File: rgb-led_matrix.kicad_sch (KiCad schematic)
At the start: 0 parts

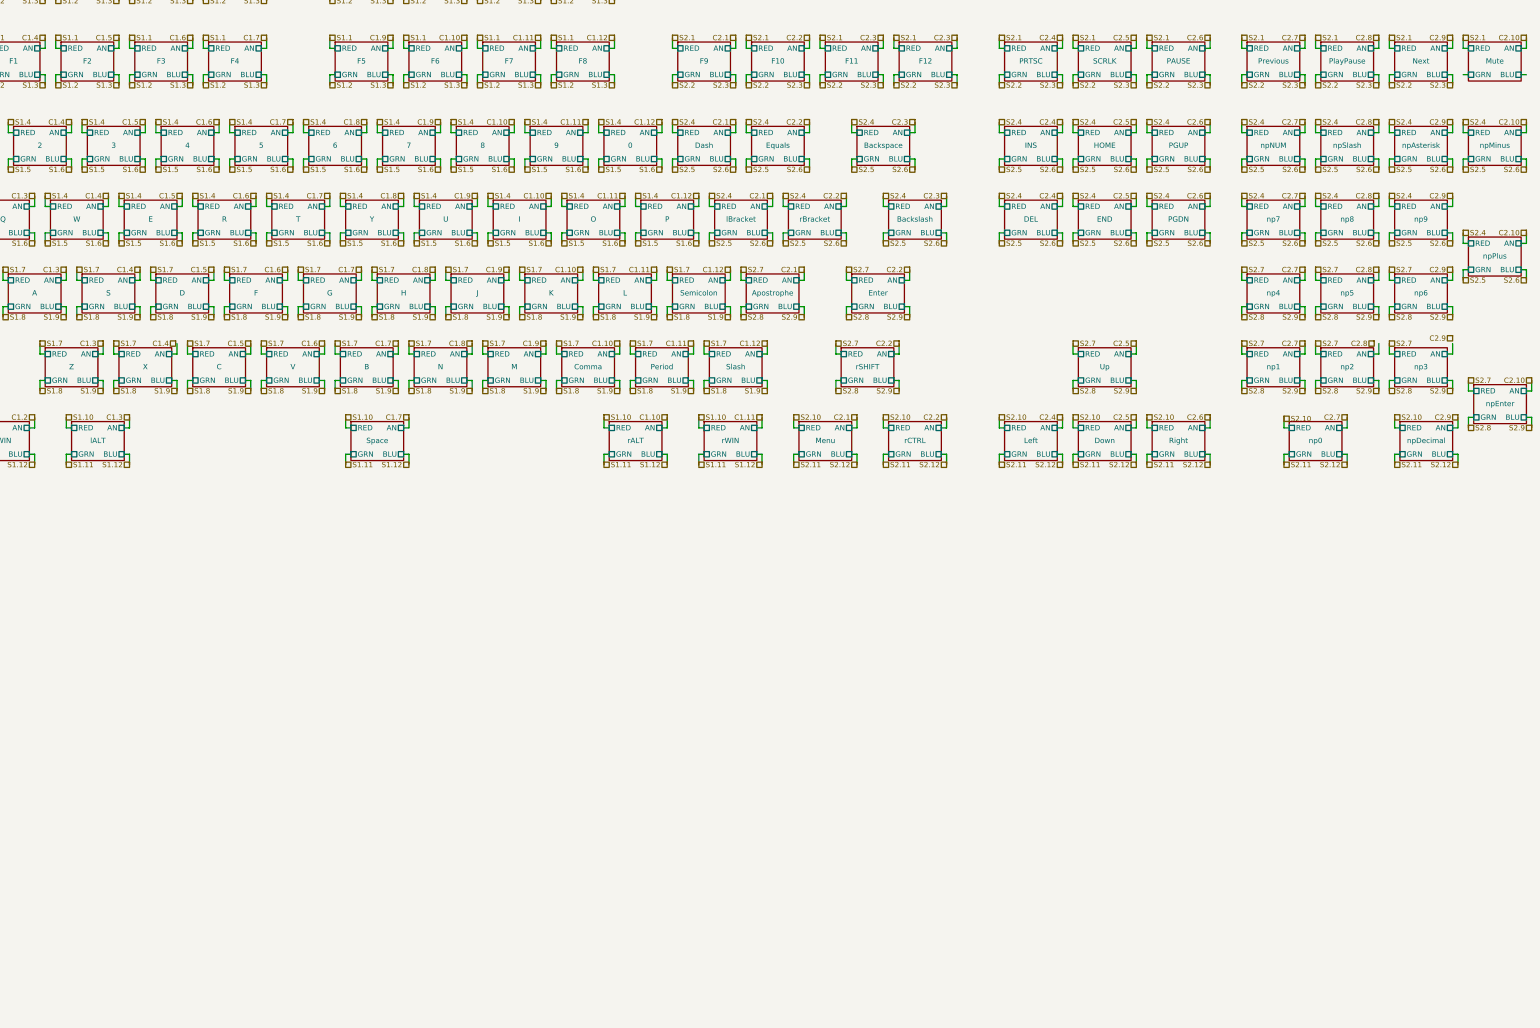
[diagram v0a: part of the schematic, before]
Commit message: Minor pcb layout changes. Add matrix led drivers
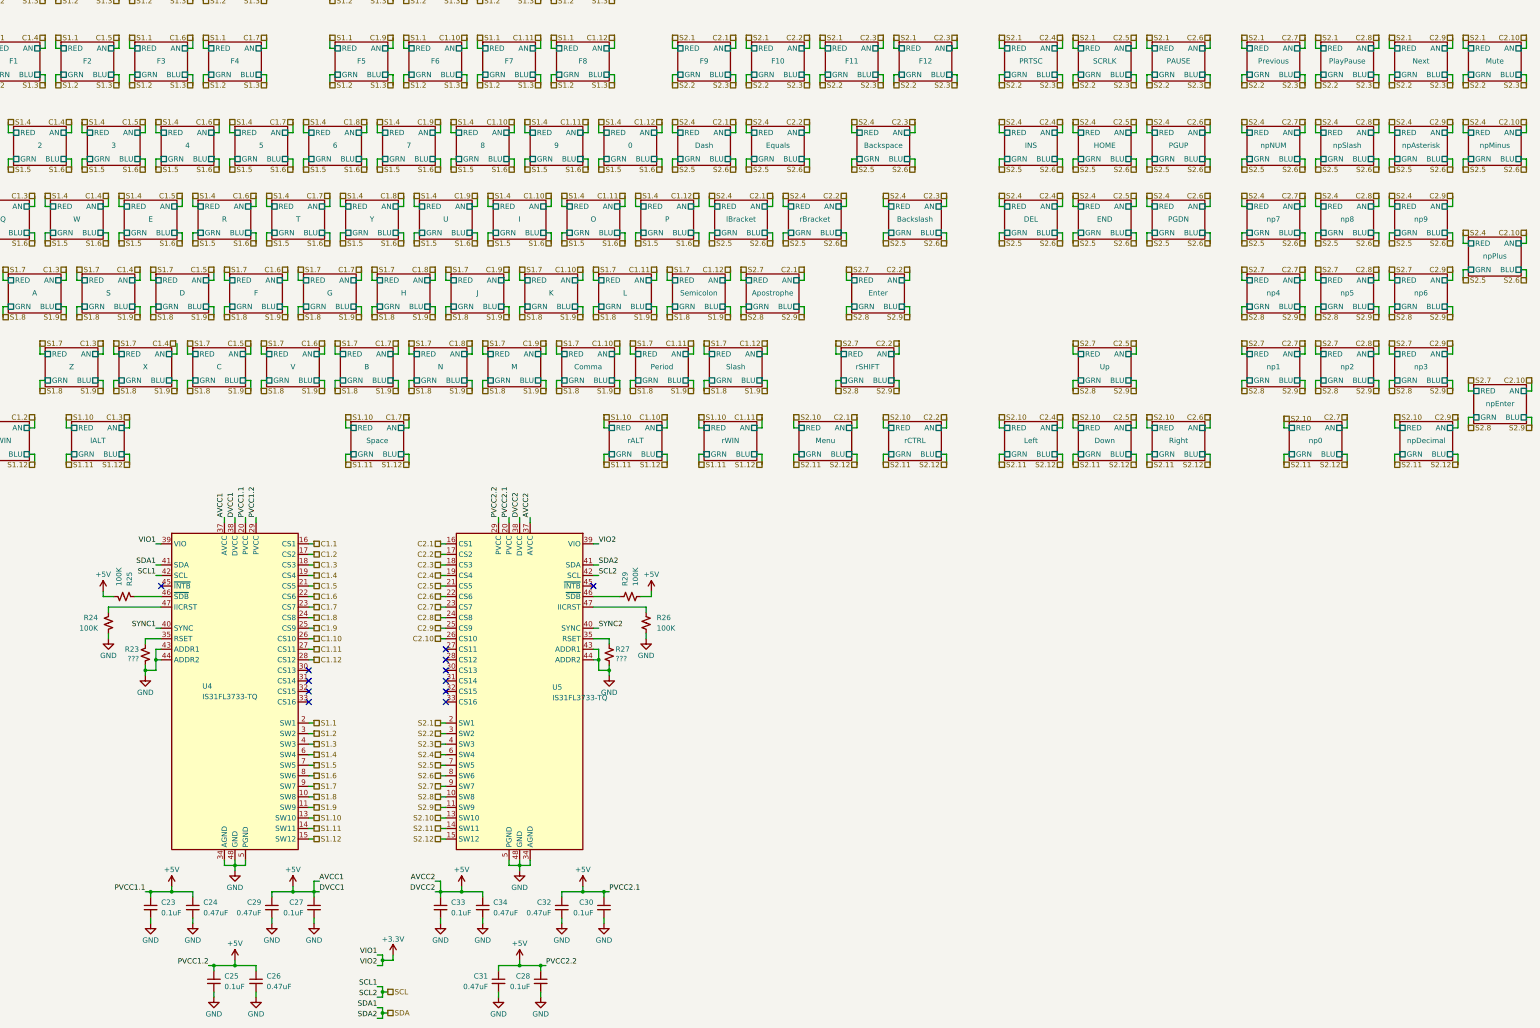
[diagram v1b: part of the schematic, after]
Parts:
- added C23, C25, C27, C28, C30, C33: 0.1uF, symbol Device:C_Small
- added C24, C26, C29, C31, C32, C34: 0.47uF, symbol Device:C_Small
- added R23, R27: ???, symbol Device:R_Small_US
- added R24, R25, R26, R29: 100K, symbol Device:R_Small_US
- added U4, U5: IS31FL3733-TQ, Package_QFP:TQFP-48-1EP_7x7mm_P0.5mm_EP5x5mm, symbol Driver_LED:IS31FL3733-TQ
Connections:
- net C1.1: now also U4.16 (CS1)
- net C1.10: now also U4.26 (CS10)
- net C1.11: now also U4.27 (CS11)
- net C1.12: now also U4.28 (CS12)
- net C1.2: now also U4.17 (CS2)
- net C1.3: now also U4.18 (CS3)
- net C1.4: now also U4.19 (CS4)
- net C1.5: now also U4.21 (CS5)
- net C1.6: now also U4.22 (CS6)
- net C1.7: now also U4.23 (CS7)
- net C1.8: now also U4.24 (CS8)
- net C1.9: now also U4.25 (CS9)
- net C2.1: now also U5.16 (CS1)
- net C2.10: now also U5.26 (CS10)
- net C2.2: now also U5.17 (CS2)
- net C2.3: now also U5.18 (CS3)
- net C2.4: now also U5.19 (CS4)
- net C2.5: now also U5.21 (CS5)
- net C2.6: now also U5.22 (CS6)
- net C2.7: now also U5.23 (CS7)
- net C2.8: now also U5.24 (CS8)
- net C2.9: now also U5.25 (CS9)
- net S1.1: now also U4.2 (SW1)
- net S1.10: now also U4.13 (SW10)
- net S1.11: now also U4.14 (SW11)
- net S1.12: now also U4.15 (SW12)
- net S1.2: now also U4.3 (SW2)
- net S1.3: now also U4.4 (SW3)
- net S1.4: now also U4.6 (SW4)
- net S1.5: now also U4.7 (SW5)
- net S1.6: now also U4.8 (SW6)
- net S1.7: now also U4.9 (SW7)
- net S1.8: now also U4.10 (SW8)
- net S1.9: now also U4.11 (SW9)
- net S2.1: now also U5.2 (SW1)
- net S2.10: now also U5.13 (SW10)
- net S2.11: now also U5.14 (SW11)
- net S2.12: now also U5.15 (SW12)
- net S2.2: now also U5.3 (SW2)
- net S2.3: now also U5.4 (SW3)
- net S2.4: now also U5.6 (SW4)
- net S2.5: now also U5.7 (SW5)
- net S2.6: now also U5.8 (SW6)
- net S2.7: now also U5.9 (SW7)
- net S2.8: now also U5.10 (SW8)
- net S2.9: now also U5.11 (SW9)
- new net: R23.1, U4.35 (RSET)
- new net: R27.1, U5.35 (RSET)
- new net: R29.1, U5.46 (~{SDB})
- new net: R26.1, U5.47 (IICRST)
- new net: R24.1, U4.47 (IICRST)
- new net: R25.1, U4.46 (~{SDB})
- new net +3.3V: U4.39 (VIO), U5.39 (VIO)
- new net +5V: C23.1, C24.1, C25.1, C26.1, C27.1, C28.1, C29.1, C30.1, C31.1, C32.1, C33.1, C34.1, R25.2, R29.2, U4.20 (PVCC), U4.29 (PVCC), U4.37 (AVCC), U4.38 (DVCC), U5.20 (PVCC), U5.29 (PVCC), U5.37 (AVCC), U5.38 (DVCC)
- new net GND: C23.2, C24.2, C25.2, C26.2, C27.2, C28.2, C29.2, C30.2, C31.2, C32.2, C33.2, C34.2, R23.2, R24.2, R26.2, R27.2, U4.12 (PGND), U4.34 (AGND), U4.43 (ADDR1), U4.44 (ADDR2), U4.48 (GND), U4.49 (GND), U4.5 (PGND), U5.12 (PGND), U5.34 (AGND), U5.43 (ADDR1), U5.44 (ADDR2), U5.48 (GND), U5.49 (GND), U5.5 (PGND)
- new net SCL: U4.42 (SCL), U5.42 (SCL)
- new net SDA: U4.41 (SDA), U5.41 (SDA)
- new net SYNC1: U4.40 (SYNC)
- new net SYNC2: U5.40 (SYNC)
- no-connect marks 0 -> 12

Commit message: led matrix work
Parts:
- removed R29: 100K, symbol Device:R_Small_US
- added C35, C36: 0.47uF, symbol Device:C_Small
- R23, R27: value ??? -> 20k
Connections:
- net SYNC2 is gone; now on net SYNC: U5.40 (SYNC)
- net +3.3V: now also C27.1, C29.1, U4.37 (AVCC), U4.38 (DVCC), C35.1, C36.1
- net +5V: no longer C23.1, C24.1, C25.1, C26.1, C27.1, C29.1, R25.2, U4.20 (PVCC), U4.29 (PVCC), U4.37 (AVCC), U4.38 (DVCC)
- net GND: now also R25.1, C35.2, C36.2
- net C2.11: now reaches U5.27 (CS11)
- net C2.12: now reaches U5.28 (CS12)
- net C2.13: now reaches U5.30 (CS13)
- net C2.14: now reaches U5.31 (CS14)
- net C2.15: now reaches U5.32 (CS15)
- net SDB: now reaches U5.46 (~{SDB})
- net SDB: now also R25.2, U4.46 (~{SDB})
- net C1.13: now reaches U4.30 (CS13)
- net C1.14: now reaches U4.31 (CS14)
- net C1.15: now reaches U4.32 (CS15)
- net C1.16: now reaches U4.33 (CS16)
- net SYNC1 renamed SYNC
- new net PVCC1.1: C23.1, C24.1, U4.20 (PVCC)
- new net PVCC1.2: C25.1, C26.1, U4.29 (PVCC)
- no-connect marks 12 -> 3
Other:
- moved on the sheet: C23, C24, C25, C26, C27, C28, C29, C30, C31, C32, C33, C34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
